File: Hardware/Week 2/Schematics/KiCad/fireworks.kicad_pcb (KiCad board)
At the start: 2 copper layers, 100.2 x 100.2 mm, 90 parts, among them J1 Conn_01x02, Q1 NPN, Q10 NPN, Q11 NPN, Q12 NPN, Q13 NPN, Q14 NPN, Q15 NPN, Q16 NPN, Q17 NPN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

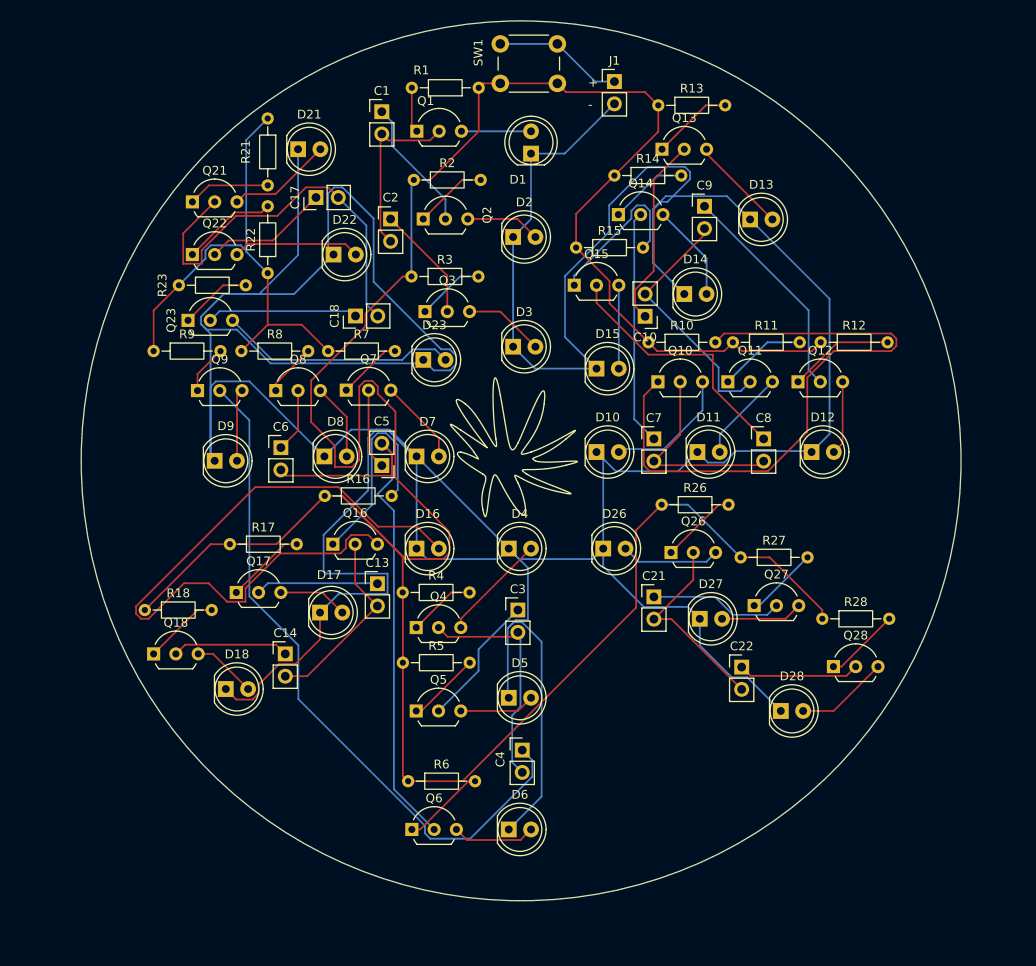
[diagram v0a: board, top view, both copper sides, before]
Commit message: Correct capacitor footprint
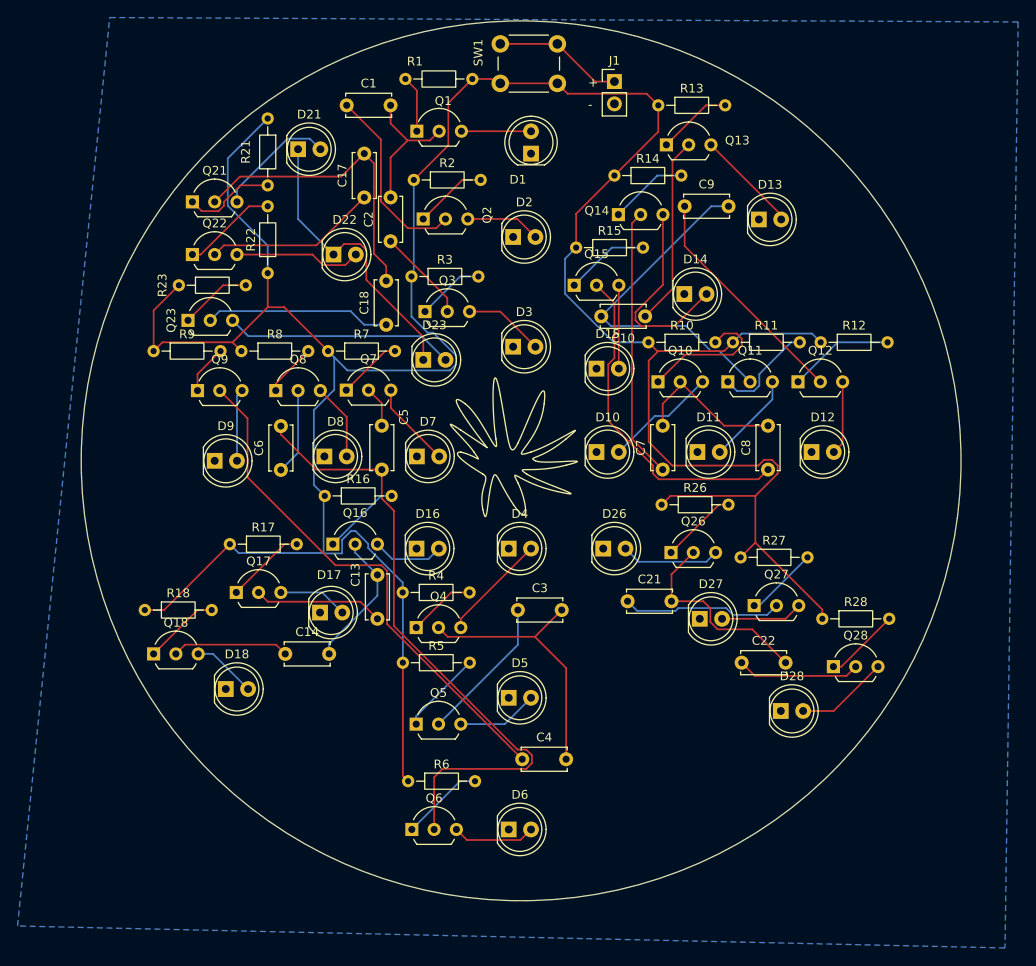
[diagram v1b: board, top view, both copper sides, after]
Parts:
- C1, C10, C13, C14, C17, C18, C2, C21, C22, C3, C4, C5, C6, C7, C8, C9: footprint Connector_PinHeader_2.54mm:PinHeader_1x02_P2.54mm_Vertical -> Capacitor_THT:C_Disc_D5.0mm_W2.5mm_P5.00mm
- moved C17 5.50 mm to (127.5, 76.0)
- moved C5 4.54 mm to (129.5, 102.0), turned to -90 degrees
- moved C1 4.07 mm to (125.5, 65.5)
- moved C13 4.00 mm to (129.0, 124.0), turned to 90 degrees
- moved C18 3.64 mm to (130.0, 90.5)
- moved C7 3.64 mm to (161.5, 107.0), turned to 90 degrees
- moved C8 3.54 mm to (173.5, 107.0), turned to 90 degrees
- moved C21 3.04 mm to (157.5, 122.0)
- moved C6 2.54 mm to (118.0, 107.0), turned to 90 degrees
- moved C2 2.54 mm to (130.5, 81.0), turned to 90 degrees
- moved C9 2.26 mm to (164.0, 77.0)
- moved Q5 1.50 mm to (133.4, 136.0)
- moved R1 1.24 mm to (139.8, 62.5)
- moved C4 1.04 mm to (145.5, 140.0)
- moved D13 1.00 mm to (172.5, 78.5)
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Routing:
- net GND: track 534.8 -> 33.4 mm
- net Net-(D16-A): track 79.1 -> 8.20 mm
- net Net-(Q10-C): track 70.9 -> 15.7 mm
- net Net-(R1-Pad1): track 376.4 -> 341.1 mm
- net Net-(Q9-B): track 79.0 -> 59.3 mm
- net Net-(Q16-C): track 23.7 -> 8.98 mm
- net Net-(D14-A): track 11.1 -> 23.2 mm
- net Net-(Q21-B): track 46.6 -> 34.9 mm
- net Net-(Q11-B): track 28.8 -> 39.7 mm
- net Net-(Q15-B): track 29.7 -> 38.5 mm
- net Net-(Q15-C): track 18.3 -> 9.62 mm
- net Net-(Q6-B): track 64.9 -> 73.0 mm
- net Net-(Q2-B): track 15.2 -> 21.6 mm
- net Net-(Q16-B): track 21.9 -> 15.8 mm
- net Net-(Q22-B): track 14.2 -> 19.7 mm
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- added copper zone on B.Cu, net GND
